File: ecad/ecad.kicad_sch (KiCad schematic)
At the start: 2 parts

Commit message: Changed EDA File
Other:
- title: (none) -> Nathan Huang
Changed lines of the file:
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@@
 	(generator_version "8.0")
 	(paper "A4")
+	(title_block
+		(title "Nathan Huang")
+		(date "2025-01-27")
+		(rev "Version 0")
+	)
 	(junction
 		(at 78.74 120.65)

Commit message: Worked on Power PCB
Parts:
- removed D1: 1N5819, Diode_THT:D_DO-41_SOD81_P10.16mm_Horizontal, symbol Diode:1N5819
- removed L1: L, symbol Device:L
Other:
- added sheet Buck Converter (Power) (Buck_Converter.kicad_sch)
- added sheet Front Panel (Front_Panel_sch.kicad_sch)

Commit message: To add front panel
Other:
- sheet Buck Converter (Power) renamed Buck Converter
- added sheet Back Panel (Back_Panel_sch.kicad_sch)
- note added: "Converted Size:"
- note added: "Original Size: 17 inches (length of front panel) x 7 inches (height of front panel) x 18 inches (depth of machine)"
- title: Nathan Huang -> Buck Converter
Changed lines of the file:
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@@
 	(paper "A4")
 	(title_block
-		(title "Nathan Huang")
+		(title "Buck Converter")
 		(date "2025-01-27")
-		(rev "Version 0")
+		(rev "Team 15")
+	)
+	(text "Converted Size:\n"
+		(exclude_from_sim no)
+		(at 21.59 166.116 0)
+		(effects
+			(font
+				(size 1.27 1.27)
+			)
+		)
+	)
+	(text "Original Size: 17 inches (length of front panel) x 7 inches (height of front panel) x 18 inches (depth of machine)\n"
+		(exclude_from_sim no)
+		(at 71.12 157.988 0)
+		(effects
+			(font
+				(size 1.27 1.27)
+			)
+		)
 	)
 	(sheet
@@
 			(color 0 0 0 0.0000)
 		)
-		(property "Sheetname" "Buck Converter (Power)"
+		(property "Sheetname" "Buck Converter"
 			(at 16.51 15.7984 0)
 			(effects
@@
 			(project "ecad"
 				(path "/b682b302-8ca4-4b40-b0cb-fd99f4675538"
-					(page "2")
+					(page "1")
 				)
 			)
@@
 	(sheet
 		(at 69.85 16.51)
-		(size 50.8 48.26)
+		(size 50.8 45.72)
 		(fields_autoplaced yes)
 		(stroke
@@
 		)
 		(property "Sheetfile" "Front_Panel_sch.kicad_sch"
-			(at 69.85 65.3546 0)
+			(at 69.85 62.8146 0)
+			(effects
+				(font
+					(size 1.27 1.27)
+				)
+				(justify left top)
+			)
+		)
+		(instances
+			(project "ecad"
+				(path "/b682b302-8ca4-4b40-b0cb-fd99f4675538"
+					(page "2")
+				)
+			)
+		)
+	)
+	(sheet
+		(at 127 16.51)
+		(size 48.26 45.72)
+		(fields_autoplaced yes)
+		(stroke
+			(width 0.1524)
+			(type solid)
+		)
+		(fill
+			(color 0 0 0 0.0000)
+		)
+		(property "Sheetname" "Back Panel"
+			(at 127 15.7984 0)
+			(effects
+				(font
+					(size 1.27 1.27)
+				)
+				(justify left bottom)
+			)
+		)
+		(property "Sheetfile" "Back_Panel_sch.kicad_sch"
+			(at 127 62.8146 0)
 			(effects
 				(font
@@
 	(sheet_instances
 		(path "/"
-			(page "1")
+			(page "0")
 		)
 	)

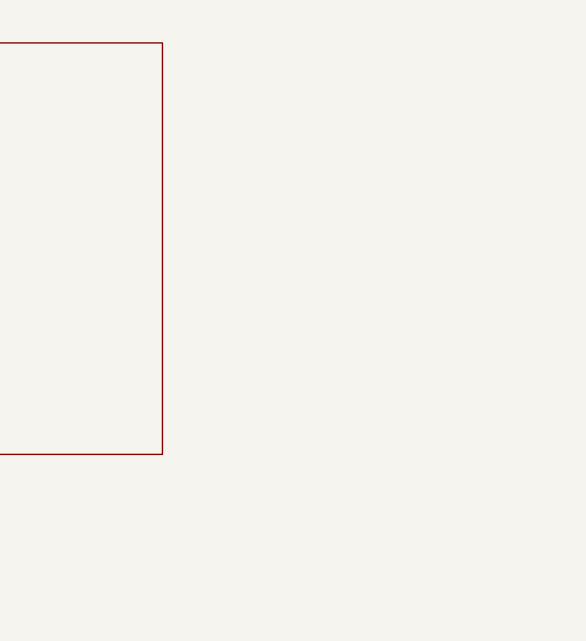
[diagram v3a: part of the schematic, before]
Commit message: Started Front Panel
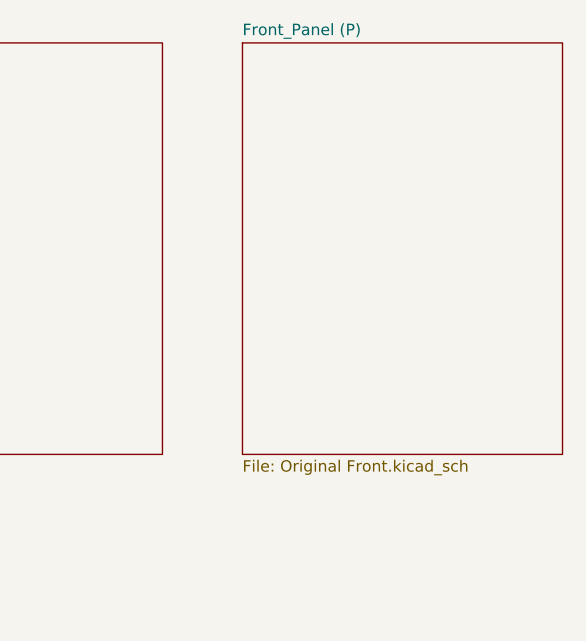
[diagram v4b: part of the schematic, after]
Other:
- added sheet Front_Panel (P) (Original Front.kicad_sch)
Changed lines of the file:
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@@
+	)
+	(sheet
+		(at 184.15 16.51)
+		(size 35.56 45.72)
+		(fields_autoplaced yes)
+		(stroke
+			(width 0.1524)
+			(type solid)
+		)
+		(fill
+			(color 0 0 0 0.0000)
+		)
+		(property "Sheetname" "Front_Panel (P)"
+			(at 184.15 15.7984 0)
+			(effects
+				(font
+					(size 1.27 1.27)
+				)
+				(justify left bottom)
+			)
+		)
+		(property "Sheetfile" "Original Front.kicad_sch"
+			(at 184.15 62.8146 0)
+			(effects
+				(font
+					(size 1.27 1.27)
+				)
+				(justify left top)
+			)
+		)
+		(instances
+			(project "ecad"
+				(path "/b682b302-8ca4-4b40-b0cb-fd99f4675538"
+					(page "5")
+				)
+			)
+		)
 	)
 	(sheet

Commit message: initial card schematic
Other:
- added sheet Card (Card.kicad_sch)
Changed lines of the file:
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@@
+		)
+	)
+	(sheet
+		(at 232.41 16.51)
+		(size 46.99 45.72)
+		(fields_autoplaced yes)
+		(stroke
+			(width 0.1524)
+			(type solid)
+		)
+		(fill
+			(color 0 0 0 0.0000)
+		)
+		(property "Sheetname" "Card"
+			(at 232.41 15.7984 0)
+			(effects
+				(font
+					(size 1.27 1.27)
+				)
+				(justify left bottom)
+			)
+		)
+		(property "Sheetfile" "Card.kicad_sch"
+			(at 232.41 62.8146 0)
+			(effects
+				(font
+					(size 1.27 1.27)
+				)
+				(justify left top)
+			)
+		)
+		(instances
+			(project "ecad"
+				(path "/b682b302-8ca4-4b40-b0cb-fd99f4675538"
+					(page "6")
+				)
+			)
 		)
 	)

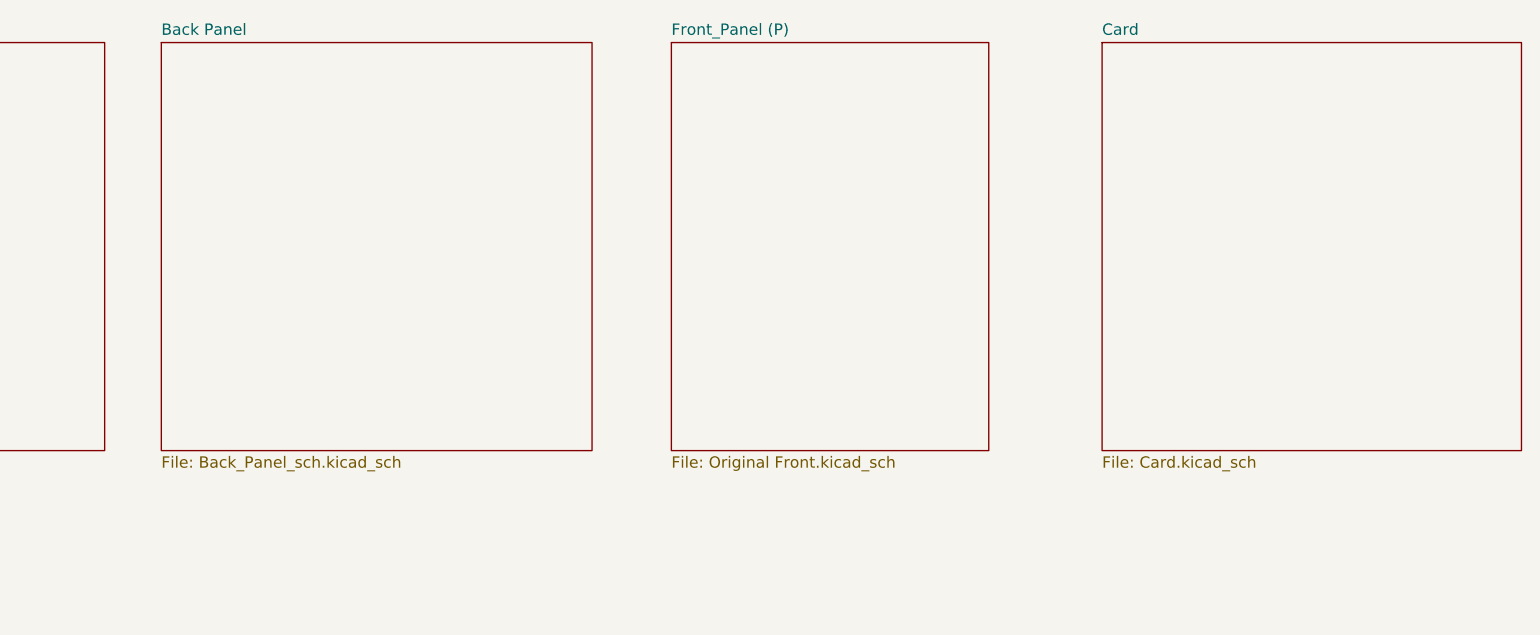
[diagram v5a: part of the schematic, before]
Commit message: lib additions
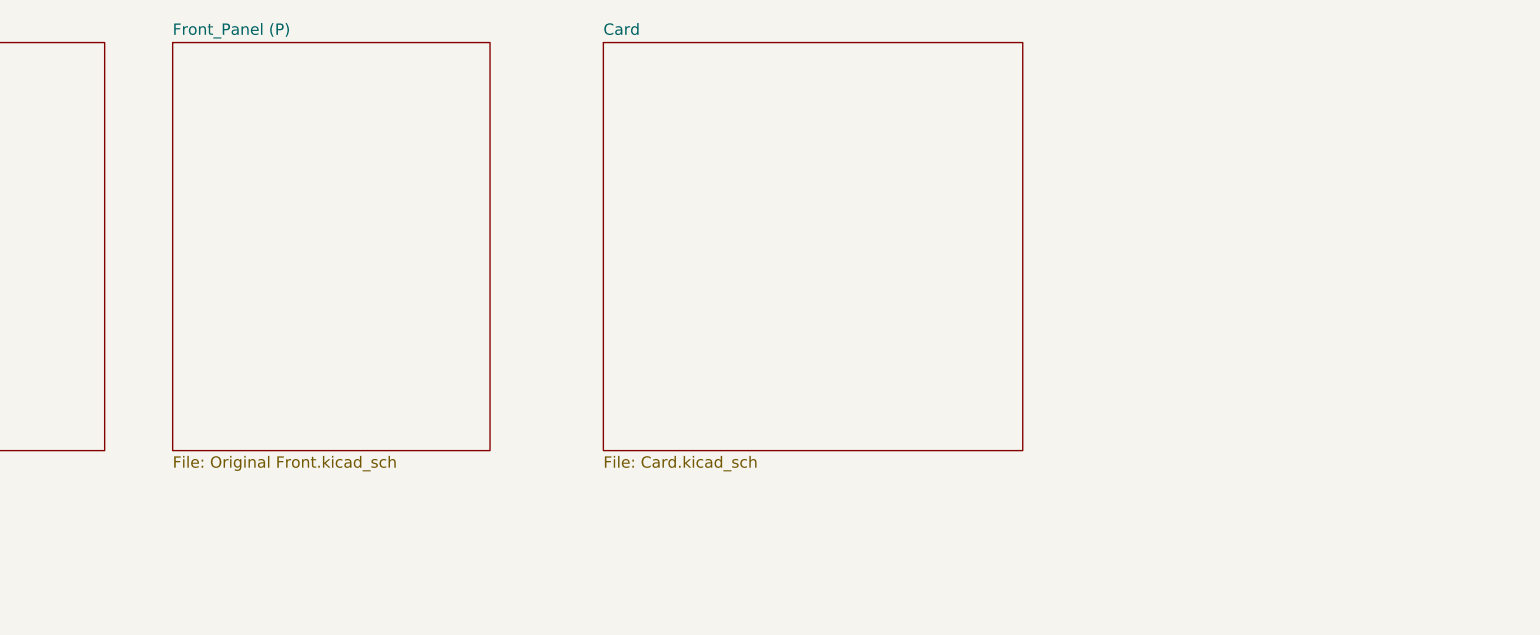
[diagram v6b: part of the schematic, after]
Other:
- removed sheet Back Panel
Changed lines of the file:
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@@
 	)
 	(sheet
-		(at 184.15 16.51)
+		(at 128.27 16.51)
 		(size 35.56 45.72)
 		(fields_autoplaced yes)
@@
 		)
 		(property "Sheetname" "Front_Panel (P)"
-			(at 184.15 15.7984 0)
+			(at 128.27 15.7984 0)
 			(effects
 				(font
@@
 		)
 		(property "Sheetfile" "Original Front.kicad_sch"
-			(at 184.15 62.8146 0)
+			(at 128.27 62.8146 0)
 			(effects
 				(font
@@
 	)
 	(sheet
-		(at 127 16.51)
-		(size 48.26 45.72)
-		(fields_autoplaced yes)
-		(stroke
-			(width 0.1524)
-			(type solid)
-		)
-		(fill
-			(color 0 0 0 0.0000)
-		)
-		(property "Sheetname" "Back Panel"
-			(at 127 15.7984 0)
-			(effects
-				(font
-					(size 1.27 1.27)
-				)
-				(justify left bottom)
-			)
-		)
-		(property "Sheetfile" "Back_Panel_sch.kicad_sch"
-			(at 127 62.8146 0)
-			(effects
-				(font
-					(size 1.27 1.27)
-				)
-				(justify left top)
-			)
-		)
-		(instances
-			(project "ecad"
-				(path "/b682b302-8ca4-4b40-b0cb-fd99f4675538"
-					(page "3")
-				)
-			)
-		)
-	)
-	(sheet
-		(at 232.41 16.51)
+		(at 176.53 16.51)
 		(size 46.99 45.72)
 		(fields_autoplaced yes)
@@
 		)
 		(property "Sheetname" "Card"
-			(at 232.41 15.7984 0)
+			(at 176.53 15.7984 0)
 			(effects
 				(font
@@
 		)
 		(property "Sheetfile" "Card.kicad_sch"
-			(at 232.41 62.8146 0)
+			(at 176.53 62.8146 0)
 			(effects
 				(font
